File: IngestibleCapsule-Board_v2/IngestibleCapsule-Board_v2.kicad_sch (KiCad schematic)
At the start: 4 parts, among them J2 AXF6K0412A, J3 AXF5K0412A, J4 513389873, J5 559099872

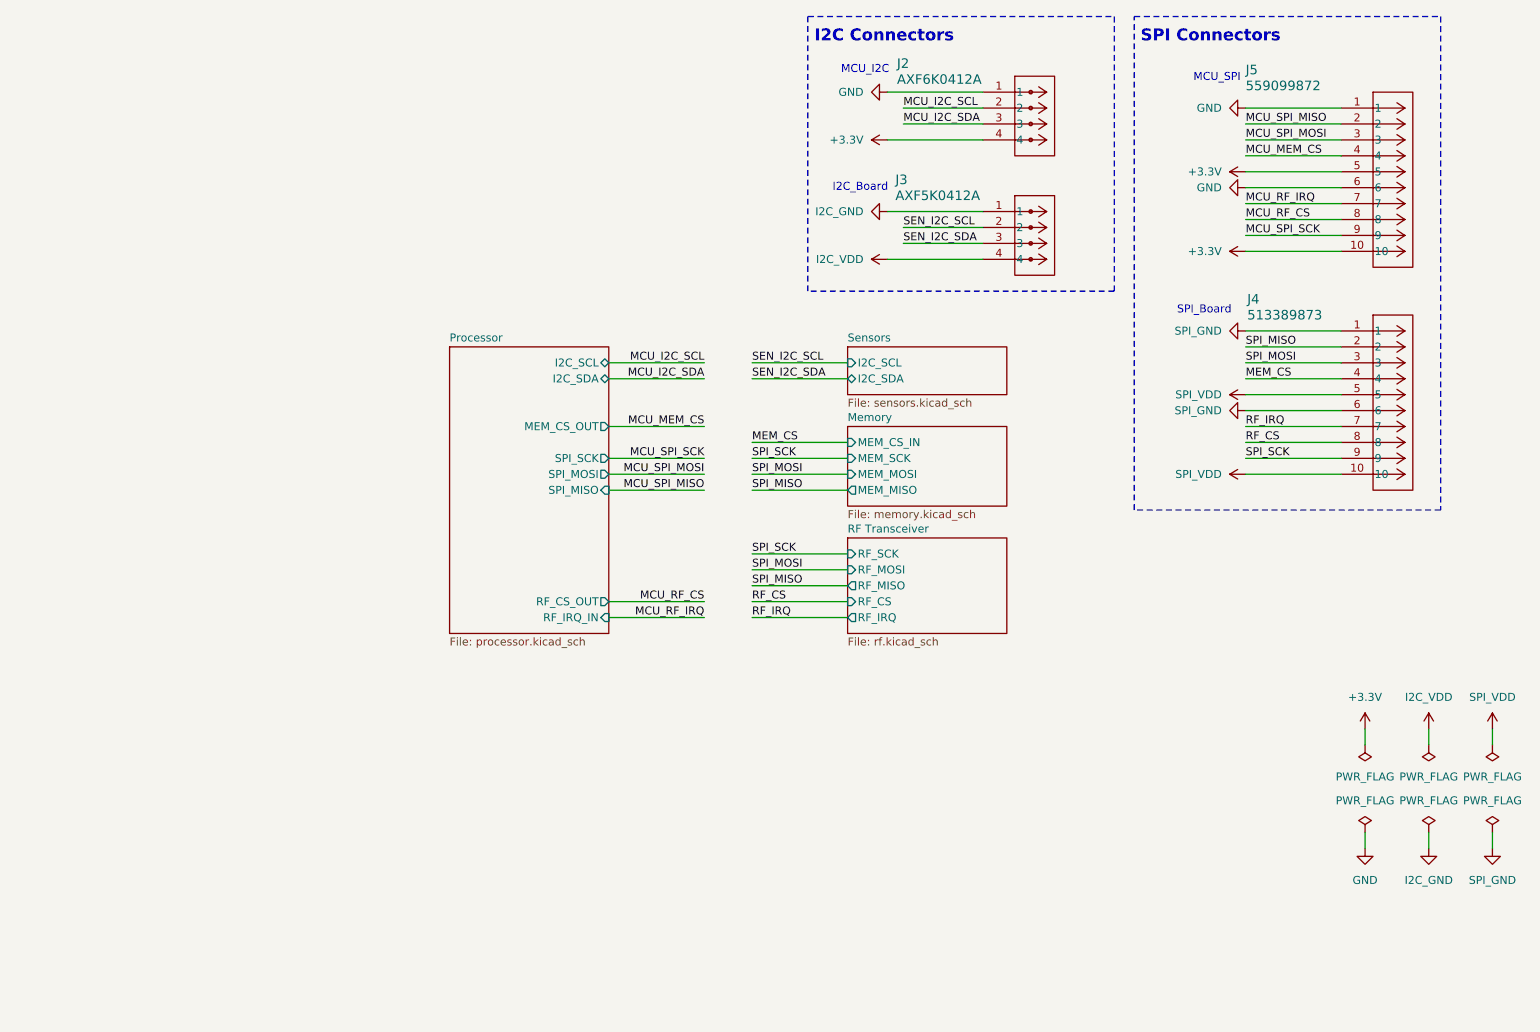
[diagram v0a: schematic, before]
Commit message: full v2 implementation, has 5 circles connected by mousebites
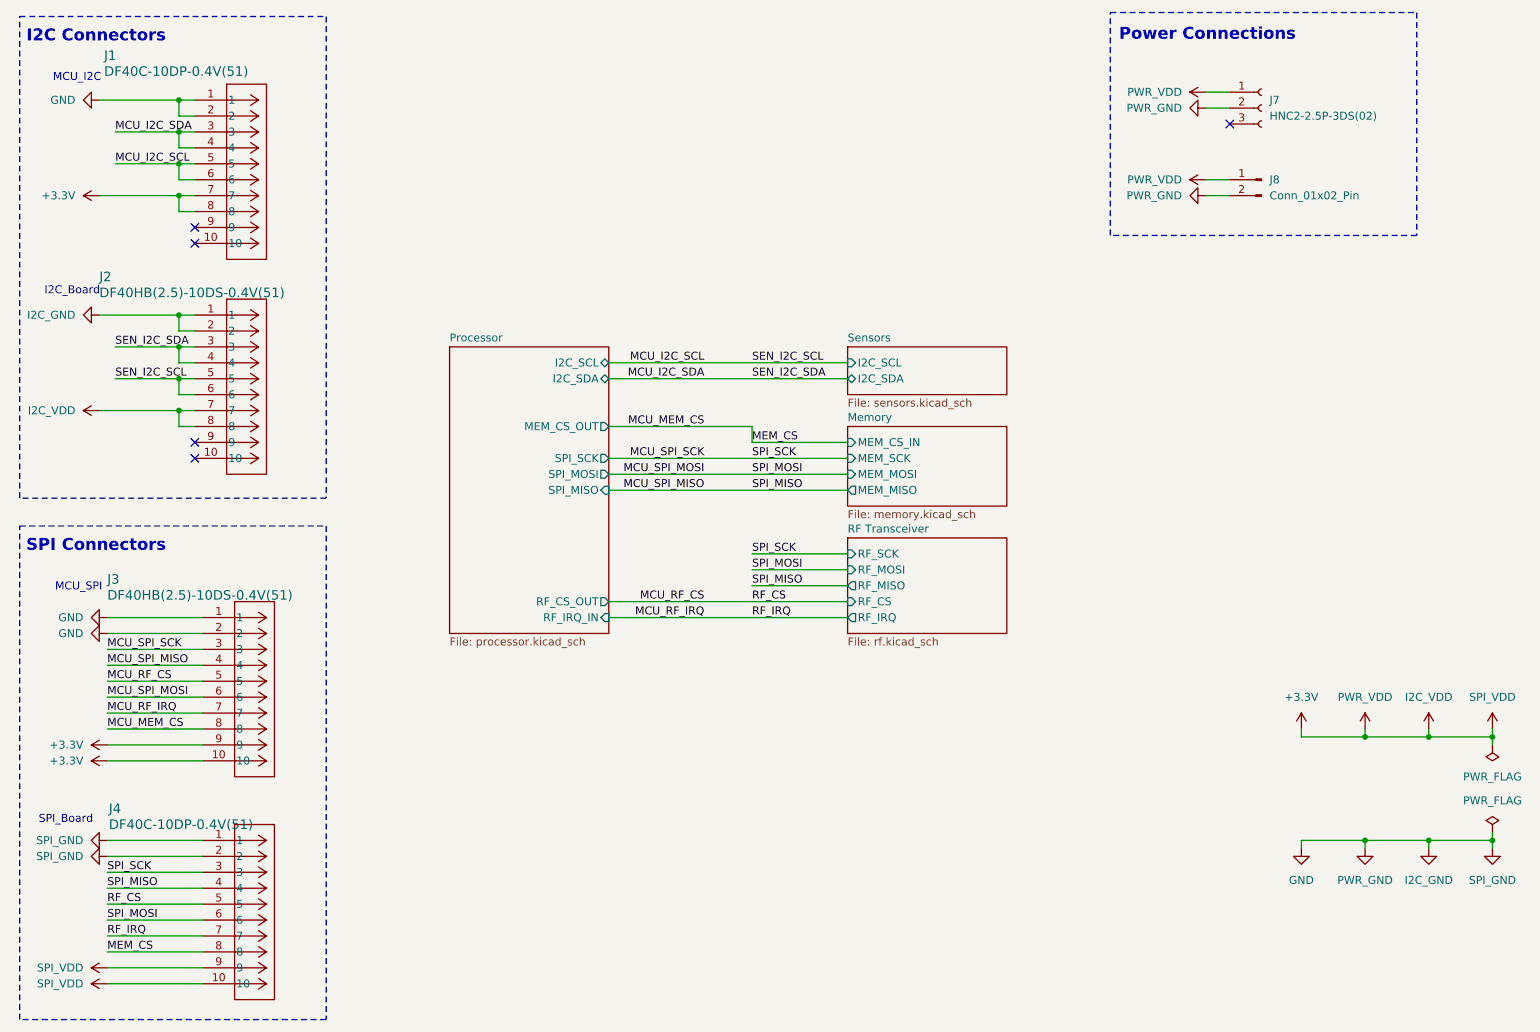
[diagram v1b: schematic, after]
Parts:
- removed J2: AXF6K0412A, kjp_fplib:AXF6K0412A, symbol kjp_symlib:AXF6K0412A
- removed J3: AXF5K0412A, kjp_fplib:AXF5K0412A, symbol kjp_symlib:AXF5K0412A
- added J1: DF40C-10DP-0.4V(51), kjp_fplib:DF40C-10DP-0.4V(51), symbol kjp_symlib:513389873
- added J2: DF40HB(2.5)-10DS-0.4V(51), kjp_fplib:DF40HB(2.5)-10DS-0.4V(51), symbol kjp_symlib:559099872
- added J7: HNC2-2.5P-3DS(02), kjp_fplib:HNC2-2.5P-3DS(02), symbol Connector:Conn_01x03_Socket
- added J8: Conn_01x02_Pin, Connector_PinSocket_2.54mm:PinSocket_1x02_P2.54mm_Vertical, symbol Connector:Conn_01x02_Pin
- J3: renamed from J5; value 559099872 -> DF40HB(2.5)-10DS-0.4V(51); footprint kjp_fplib:CON_559099872 -> kjp_fplib:DF40HB(2.5)-10DS-0.4V(51)
- J4: value 513389873 -> DF40C-10DP-0.4V(51); footprint kjp_fplib:CON_513389873 -> kjp_fplib:DF40C-10DP-0.4V(51)
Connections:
- net MEM_CS is gone; now on net MCU_SPI_MISO: J4.4
- net RF_CS is gone; now on net MCU_MEM_CS: J4.8
- net RF_IRQ is gone; now on net MCU_RF_IRQ: J4.7
- net SPI_MISO is gone; now on net GND: J4.2
- net SPI_MOSI is gone; now on net MCU_SPI_SCK: J4.3
- net SPI_SCK is gone; now on net +3.3V: J4.9
- net +3.3V: now also J3.9, J4.10, J1.7, J1.8, J2.7, J2.8, J7.1 (Pin_1), J8.1 (Pin_1); no longer J3.5
- net GND: now also J3.2, J4.1, J1.1, J1.2, J2.1, J2.2, J7.2 (Pin_2), J8.2 (Pin_2); no longer J3.6
- net MCU_I2C_SCL: now also J1.5, J1.6, J2.5, J2.6
- net MCU_I2C_SDA: now also J1.3, J1.4, J2.3, J2.4
- net MCU_MEM_CS: now also J3.8; no longer J3.4
- net MCU_RF_CS: now also J3.5, J4.5; no longer J3.8
- net MCU_SPI_MISO: now also J3.4; no longer J3.2
- net MCU_SPI_MOSI: now also J3.6, J4.6; no longer J3.3
- net MCU_SPI_SCK: now also J3.3; no longer J3.9
- removed net SPI_GND: J4.1, J4.6
- removed net SPI_VDD: J4.10, J4.5
- no-connect marks 0 -> 5
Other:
- note added: "Power Connections"
- moved on the sheet: J3, J4
